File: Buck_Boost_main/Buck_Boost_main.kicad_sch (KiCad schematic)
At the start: 0 parts

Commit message: test
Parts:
- added U1: 4001, symbol 4xxx:4001
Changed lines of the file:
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@@
 	(generator_version "9.0")
 	(paper "A4")
+	(symbol
+		(lib_id "4xxx:4001")
+		(at 116.84 102.87 0)
+		(unit 1)
+		(exclude_from_sim no)
+		(in_bom yes)
+		(on_board yes)
+		(dnp no)
+		(fields_autoplaced yes)
+		(property "Reference" "U1"
+			(at 116.84 93.98 0)
+			(effects
+				(font
+					(size 1.27 1.27)
+				)
+			)
+		)
+		(property "Value" "4001"
+			(at 116.84 96.52 0)
+			(effects
+				(font
+					(size 1.27 1.27)
+				)
+			)
+		)
+		(property "Footprint" ""
+			(at 116.84 102.87 0)
+			(effects
+				(font
+					(size 1.27 1.27)
+				)
+				(hide yes)
+			)
+		)
+		(property "Datasheet" "http://www.intersil.com/content/dam/Intersil/documents/cd40/cd4000bms-01bms-02bms-25bms.pdf"
+			(at 116.84 102.87 0)
+			(effects
+				(font
+					(size 1.27 1.27)
+				)
+				(hide yes)
+			)
+		)
+		(property "Description" "Quad Nor 2 inputs"
+			(at 116.84 102.87 0)
+			(effects
+				(font
+					(size 1.27 1.27)
+				)
+				(hide yes)
+			)
+		)
+		(pin "2"
+		)
+		(pin "1"
+		)
+		(pin "5"
+		)
+		(pin "3"
+		)
+		(pin "13"
+		)
+		(pin "6"
+		)
+		(pin "4"
+		)
+		(pin "8"
+		)
+		(pin "9"
+		)
+		(pin "10"
+		)
+		(pin "12"
+		)
+		(pin "7"
+		)
+		(pin "14"
+		)
+		(pin "11"
+		)
+		(instances
+			(project ""
+				(path "/fa8e210f-4539-4fad-ad3b-e2a7d22847ca"
+					(reference "U1")
+					(unit 1)
+				)
+			)
+		)
+	)
 	(sheet_instances
 		(path "/"

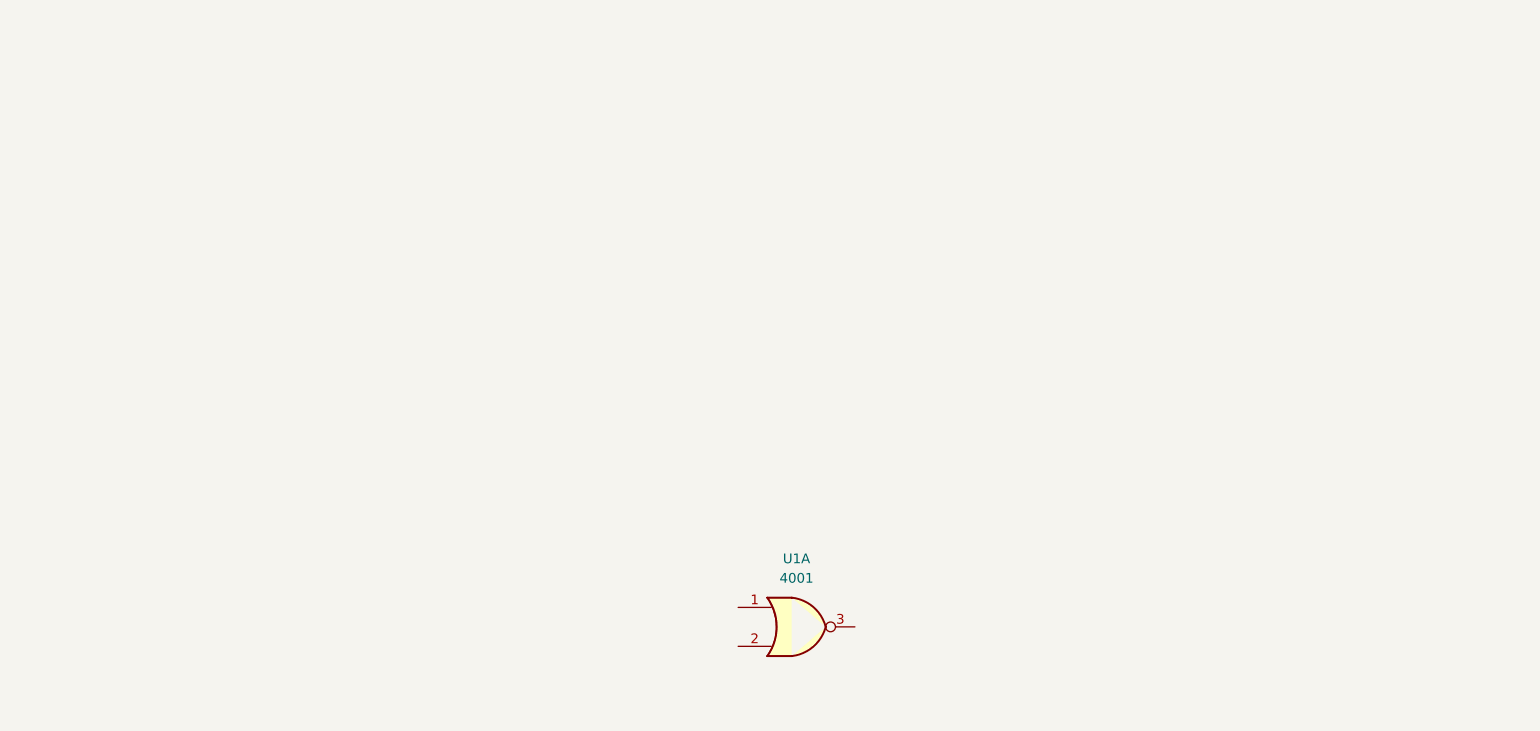
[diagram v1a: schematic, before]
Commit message: Placed in Inductor, Controller, and Fets, along with obligatory heatsink, screw terms, and fuses.
I realized that we already have an extra 15uh power inductor from the bucks with very low dcr and high sat current (1.62mohm, 16A), so we can use this one:(PQ2614BHA-150K)
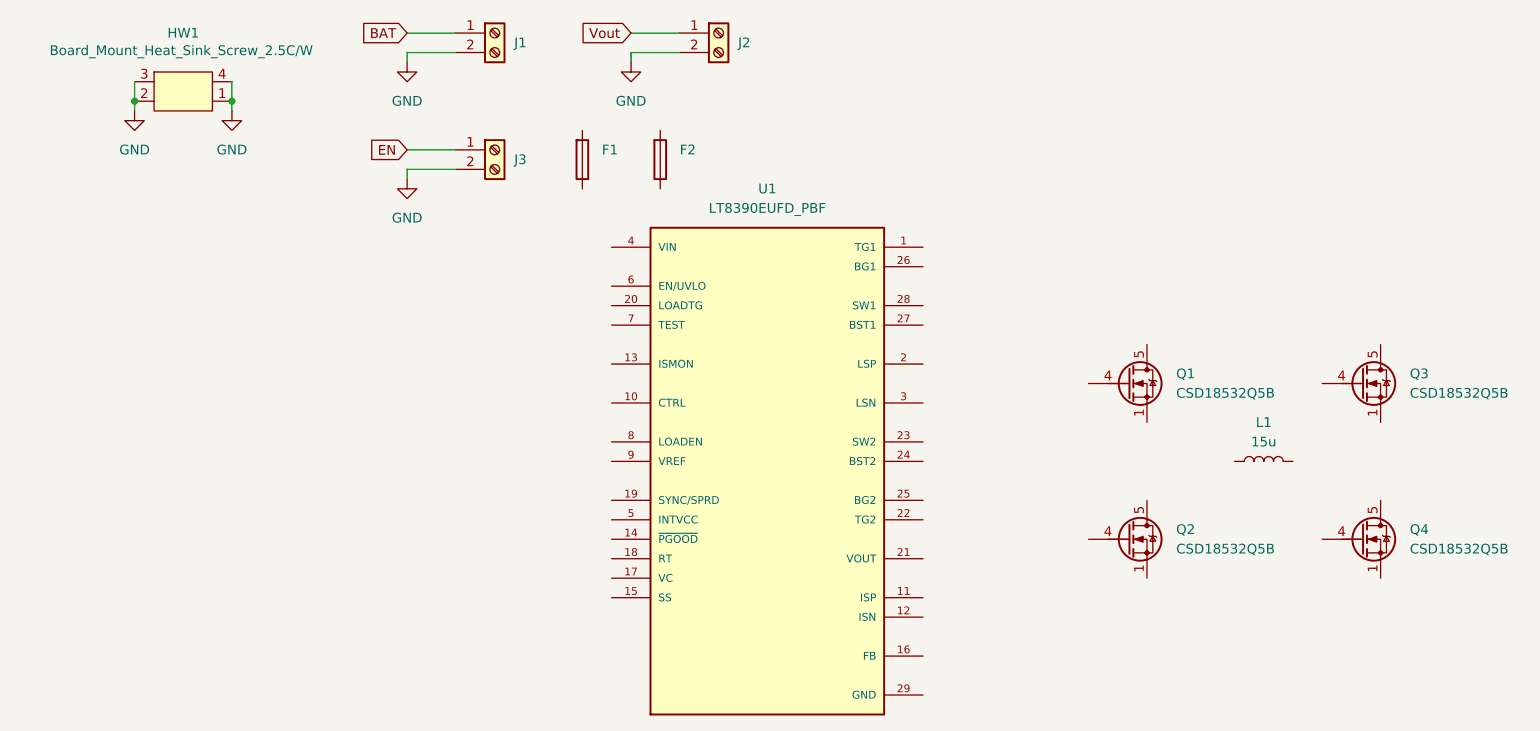
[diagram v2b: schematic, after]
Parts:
- removed U1: 4001, symbol 4xxx:4001
- added F1, F2: Fuse_Holder_Auto, rsx_fuses:FUSE_3568-10, symbol rsx_fuses:Fuse_Holder_Auto
- added HW1: Board_Mount_Heat_Sink_Screw_2.5C/W, rsx_misc:ATS-1139-C1-R0, symbol rsx_misc:Board_Mount_Heat_Sink_Screw_2.5C/W
- added J1, J2: Screw_Terminal_2x5.08, rsx_headers_screw:Molex_0398800302, symbol rsx_header_screw:Screw_Terminal_2x5.08
- added J3: Screw_Terminal_2x2.54, rsx_headers_screw:Wurth_691210910002, symbol rsx_header_screw:Screw_Terminal_2x2.54
- added L1: 15u, rsx_inductors:PQ2617BHA-XXXK, symbol rsx_inductors:15u_21A
- added Q1, Q2, Q3, Q4: CSD18532Q5B, Package_TO_SOT_SMD:TDSON-8-1, symbol Transistor_FET:CSD18532Q5B
- added U1: LT8390EUFD_PBF, LT:QFN50P500X400X80-29N, symbol LT:LT8390EUFD_PBF
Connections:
- new net: Q3.1 (S), Q3.2 (S), Q3.3 (S)
- new net: Q2.1 (S), Q2.2 (S), Q2.3 (S)
- new net: Q4.1 (S), Q4.2 (S), Q4.3 (S)
- new net: Q1.1 (S), Q1.2 (S), Q1.3 (S)
- new net BAT: J1.1 (Pin_1)
- new net EN: J3.1 (Pin_1)
- new net GND: HW1.1, HW1.2, HW1.3, HW1.4, J1.2 (Pin_2), J2.2 (Pin_2), J3.2 (Pin_2)
- new net Vout: J2.1 (Pin_1)
